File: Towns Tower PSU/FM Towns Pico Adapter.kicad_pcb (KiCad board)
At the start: 2 copper layers, 190 x 151.6 mm, 18 parts, among them J1 ATX24RH, J2 PCN13-44S-2.54DS_71_, U1 ProMicro

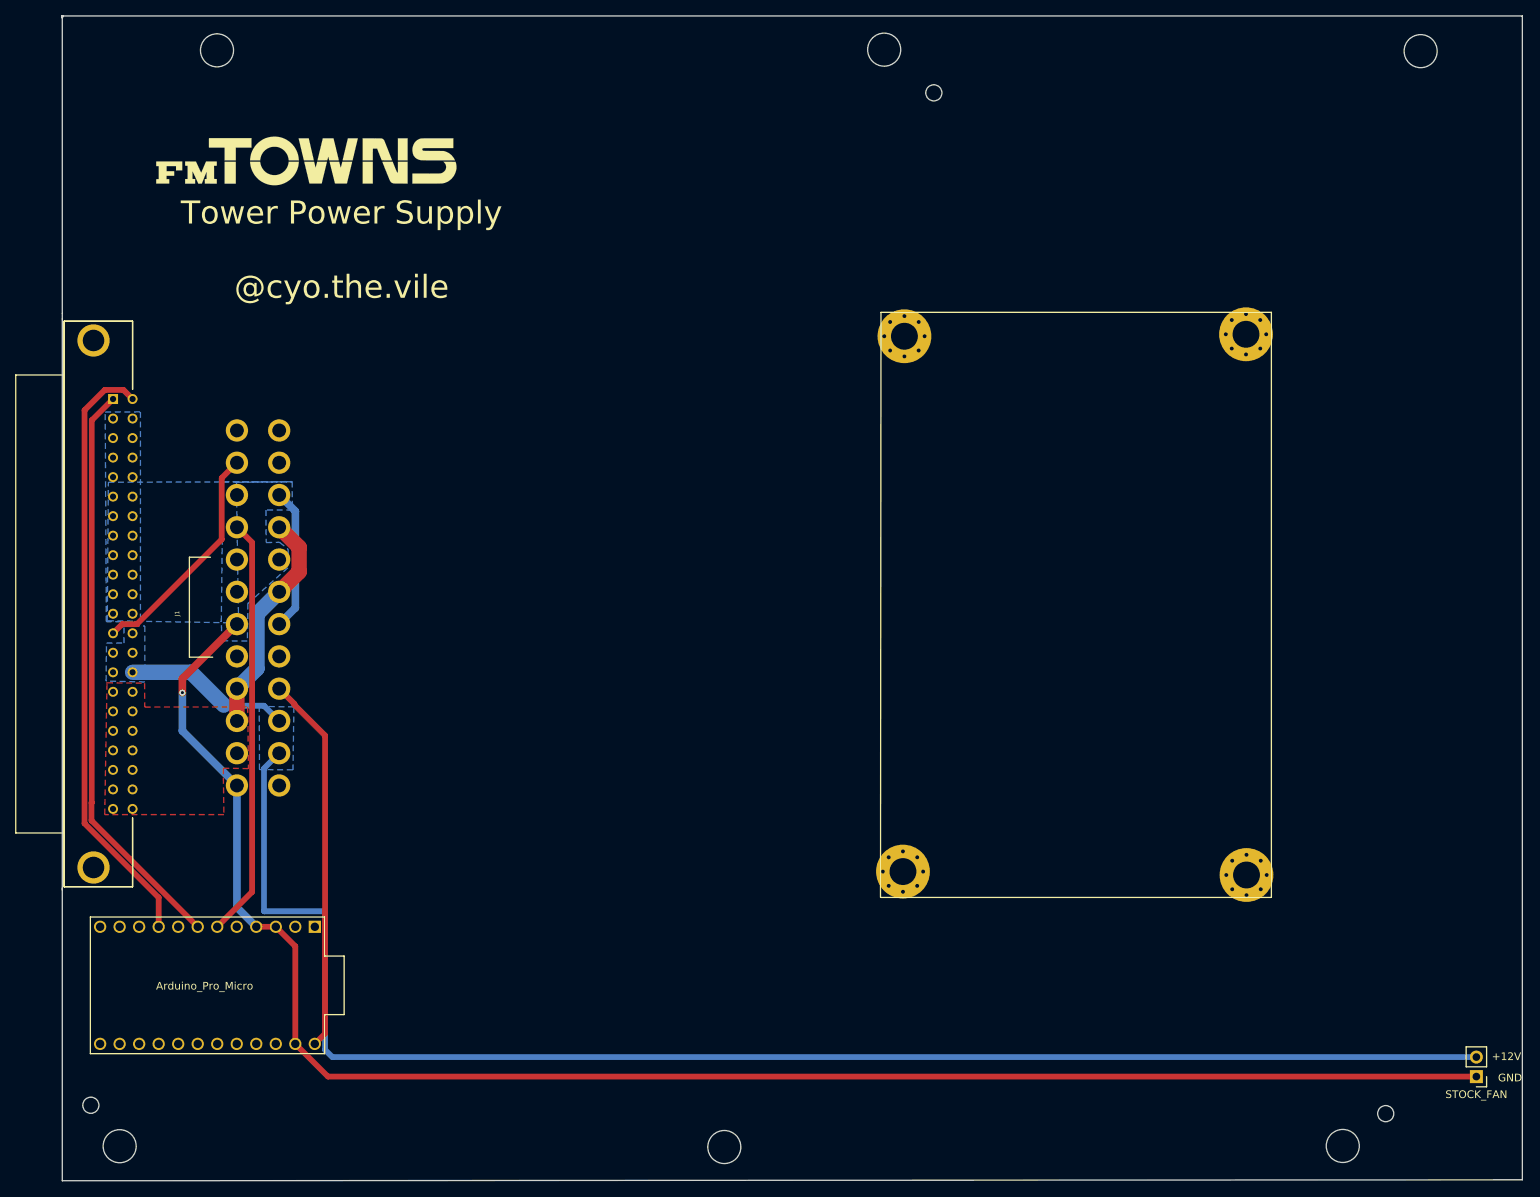
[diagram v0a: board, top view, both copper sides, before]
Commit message: Rev2
-Remeasured and added support holes for the ACDC converters in 2x4 form factor
-Verification of original mounting holes is still required
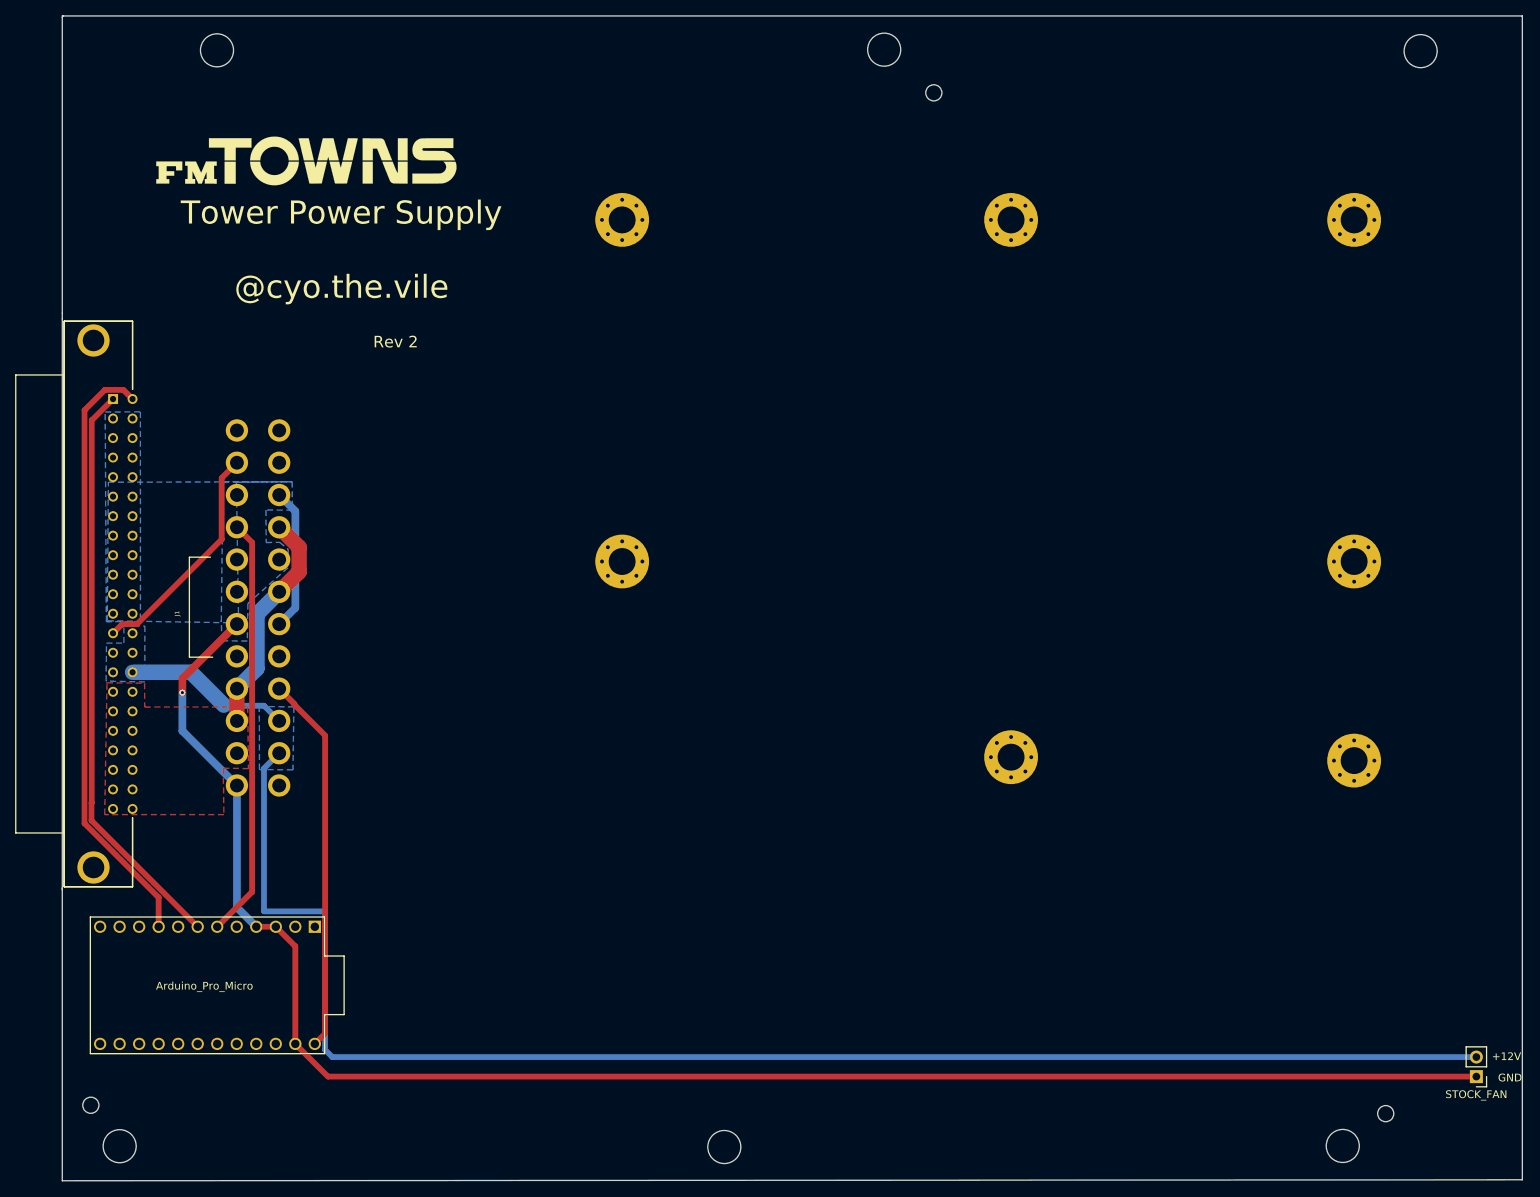
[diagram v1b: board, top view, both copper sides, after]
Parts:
- added PAD1: MountingHole_3.5mm_Pad_Via, MountingHole:MountingHole_3.5mm_Pad_Via, F.Cu at (113.0, 48.6)
- added PAD1: MountingHole_3.5mm_Pad_Via, MountingHole:MountingHole_3.5mm_Pad_Via, F.Cu at (208.2, 93.0)
- added PAD1: MountingHole_3.5mm_Pad_Via, MountingHole:MountingHole_3.5mm_Pad_Via, F.Cu at (113.0, 93.0)
- moved PAD3 20.5 mm to (163.6, 48.6)
- moved PAD4 20.5 mm to (208.2, 48.6)
- moved PAD2 20.5 mm to (163.6, 118.5)
- moved PAD1 20.4 mm to (208.2, 118.9)
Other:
- outline, holes or cut-outs redrawn
- board text added: "Rev 2"

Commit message: TownsPSU Rev3
-SLG62686 footprint added. Will add configuration file once verified on hardware although I don't see anyone using them.
-Moved fan connector since someone complained
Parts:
- added C1: 0.1uf, Capacitor_SMD:C_1206_3216Metric, F.Cu at (60.7, 151.7)
- added C2: 0.1uf, Capacitor_SMD:C_1206_3216Metric, F.Cu at (60.7, 146.1)
- added GP1: SLG46826G, SamacSys_Parts:SOP65P640X120-20N, F.Cu at (55.1, 147.6)
- moved FAN1 15.7 mm to (218.2, 145.5)
- renumbered STOCK_FAN to FAN1
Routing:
- net GND: track 239.1 -> 289.9 mm, vias 1 -> 4
- net /5V_STBY: track 49.2 -> 88.7 mm
- net +12V: track 219.0 -> 190.3 mm
- net /FM_PS_ON_N: track 79.0 -> 85.9 mm
- net /PS_ON: track 54.7 -> 59.7 mm
- net /FM_PS_OFF_N: track 75.6 -> 79.8 mm
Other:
- board text added: "5VSTBY"
- board text added: "ON/OFF"
- board text added: "OS_OFF"
- board text added: "PS_ON"
- board text added: "Rev 3"
- board text removed: "Arduino_Pro_Micro"
- board text removed: "Rev 2"
